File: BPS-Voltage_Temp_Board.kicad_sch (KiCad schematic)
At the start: 64 parts, among them J1 bms i2c test, J10 psom bms i2c test, J11 I-CAN connector, J2 voltage taps, J4 I-CAN connector, SW1 BMS_BOOT, SW2 SW_DIP_x05, U2 BQ7692003PW, U3 PeripheralSOM, U4 ISO1641BDR, U5 EL3H7, U6 EL3H7

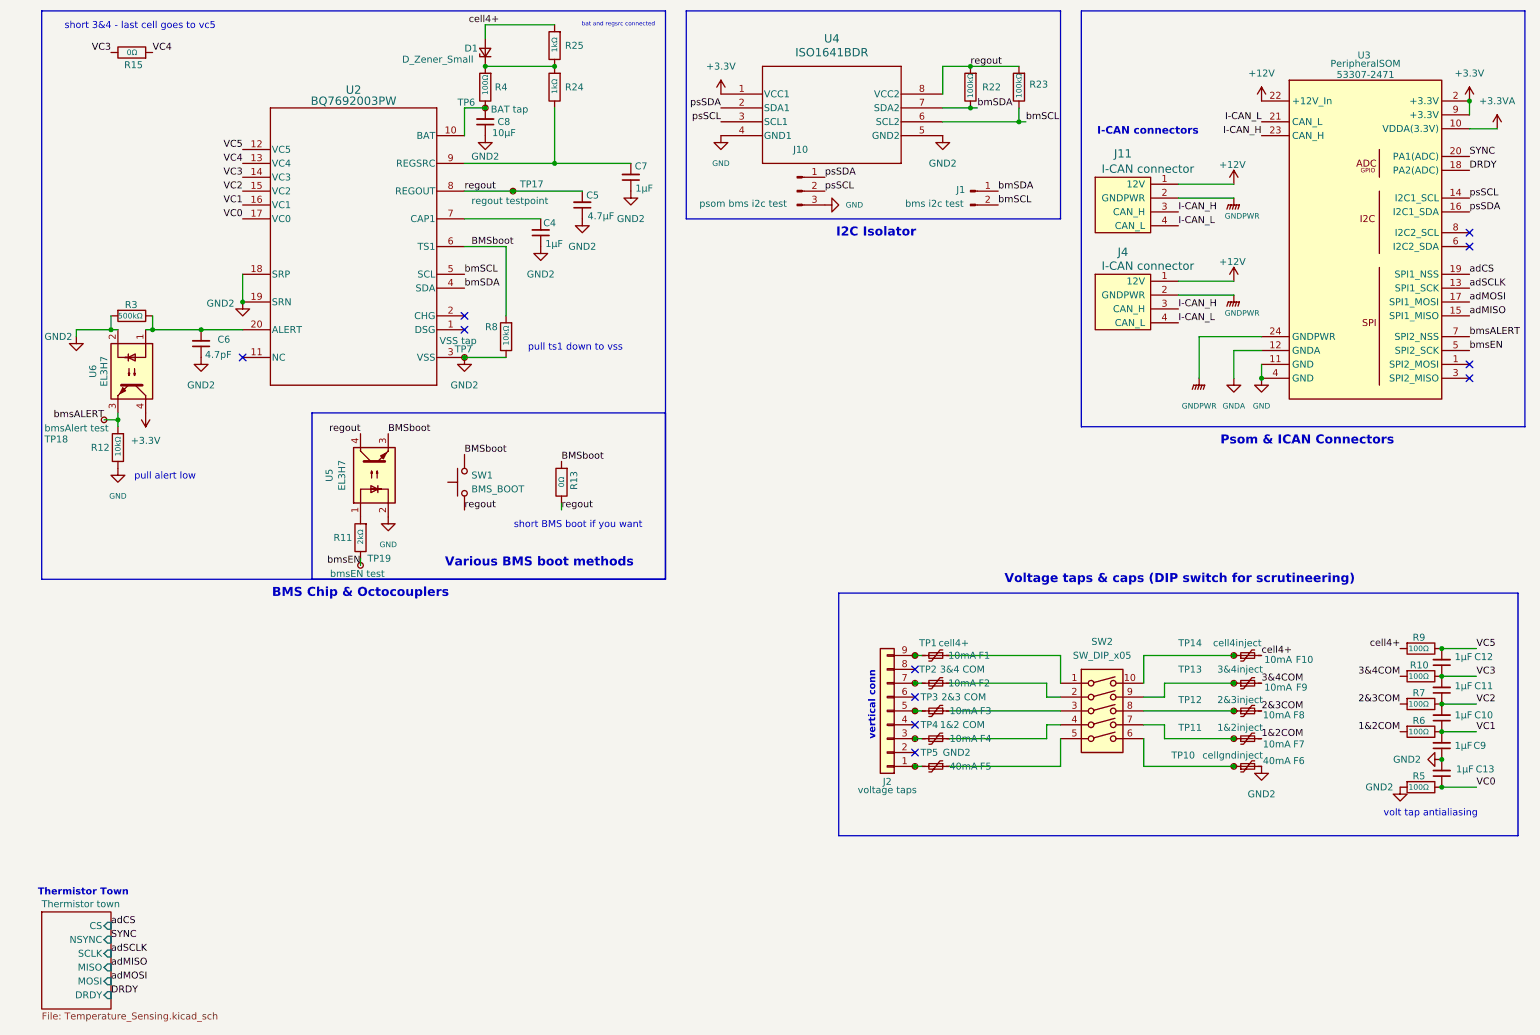
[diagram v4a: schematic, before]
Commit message: concerns from review council addressed
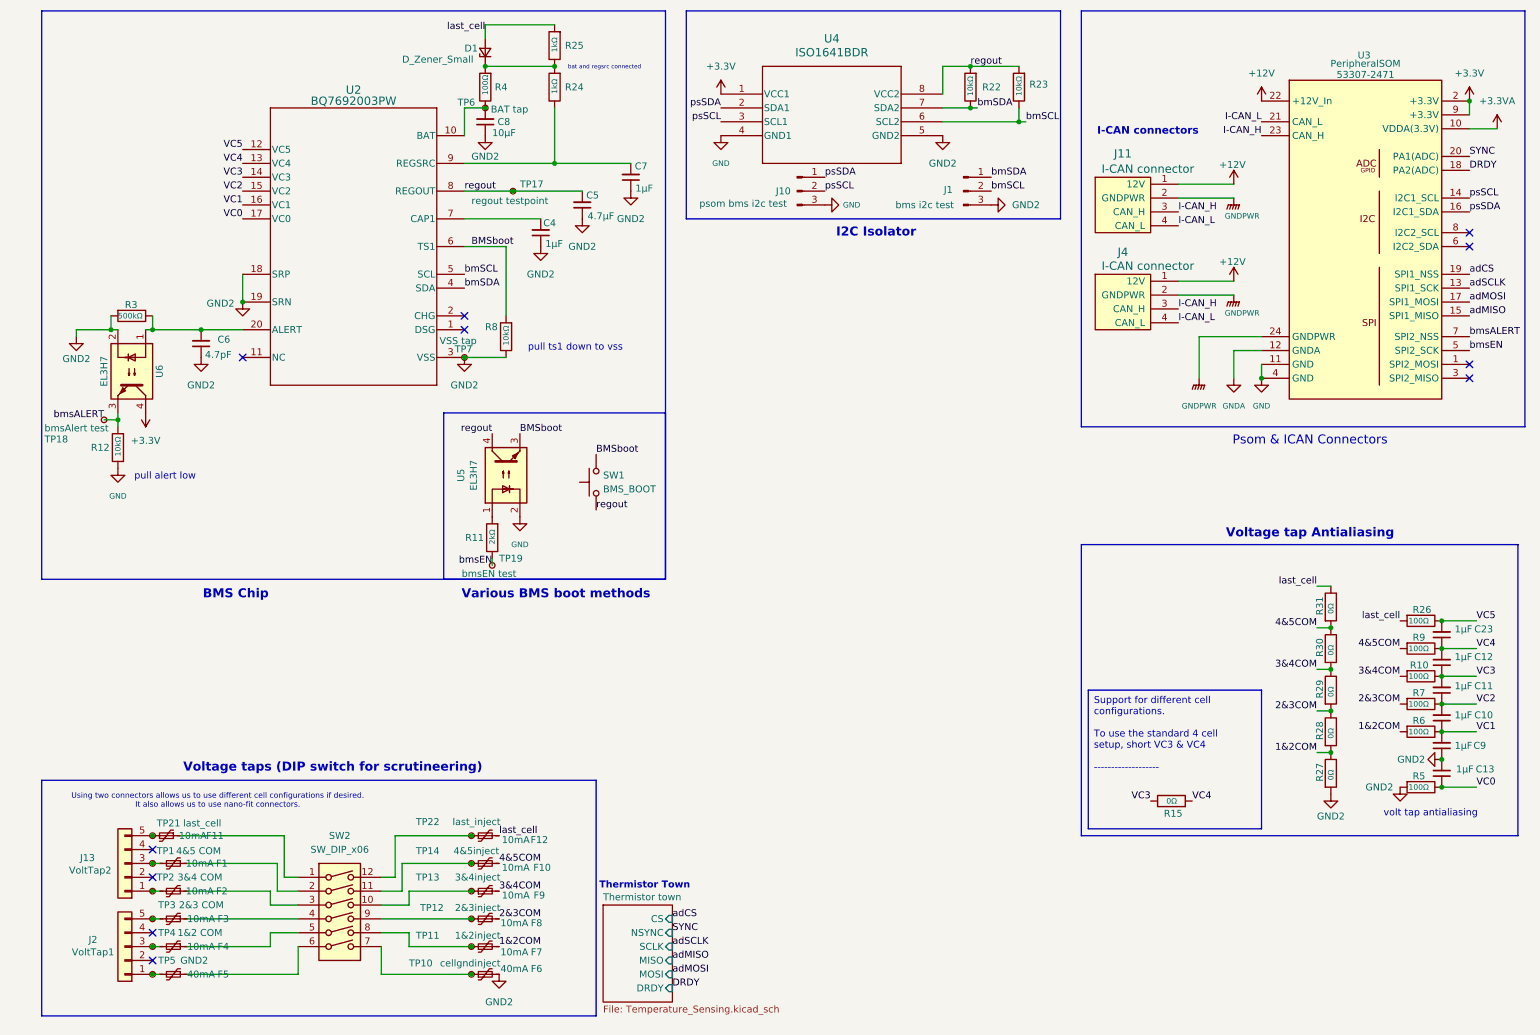
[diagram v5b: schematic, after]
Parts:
- removed J1: bms i2c test, symbol Connector:Conn_01x02_Pin
- removed J2: voltage taps, Connector_Molex:Molex_Nano-Fit_105314-xx10_2x05_P2.50mm_Horizontal, symbol Connector_Generic:Conn_01x09
- removed R13: 0Ω, Resistor_SMD:R_0805_2012Metric, symbol Device:R
- removed SW2: SW_DIP_x05, symbol Switch:SW_DIP_x05
- added C23: 1μF, Capacitor_SMD:C_0805_2012Metric, symbol Device:C_Small
- added F11, F12: 10mA, UTSVT_Special:ptc_fuse_FUSC1607X75N, symbol Device:Polyfuse_Small
- added J1: bms i2c test, symbol Connector:Conn_01x03_Pin
- added J13: VoltTap2, symbol Connector_Generic:Conn_01x05
- added J2: VoltTap1, symbol Connector_Generic:Conn_01x05
- added R26: 100Ω, Resistor_SMD:R_0805_2012Metric, symbol Device:R
- added R27, R28, R29, R30, R31: 0Ω, Resistor_SMD:R_0805_2012Metric, symbol Device:R
- added SW2: SW_DIP_x06, symbol Switch:SW_DIP_x06
- added TP21: last_cell, symbol Connector:TestPoint_Small
- added TP22: last_inject, symbol Connector:TestPoint_Small
- R22, R23: value 100kΩ -> 10kΩ
- TP1: value cell4+ -> 4&5 COM
- TP14: value cell4inject -> 4&5inject
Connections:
- net 1&2COM: now also R27.1, R28.2
- net 2&3COM: now also R28.1, R29.2
- net 3&4COM: now also R29.1, R30.2
- net GND2: now also J1.3 (Pin_3), R27.2
- net VC4: now also C12.2, R9.1, C23.1
- net VC5: now also C23.2, R26.1; no longer C12.2, R9.1
- net bmSCL: now also J1.2 (Pin_2)
- net bmSDA: now also J1.1 (Pin_1)
- net at F1.1: now also SW2.2
- net at F10.1, TP14.1: now also SW2.11
- net at F2.1: now also SW2.3
- net at F3.1: now also SW2.4
- net at F4.1: now also SW2.5
- net at F5.1: now also SW2.6
- net at F6.1, TP10.1: now also SW2.7
- net at F7.1, TP11.1: now also SW2.8
- net at F8.1, TP12.1: now also SW2.9
- net at F9.1, TP13.1: now also SW2.10
- net at F5.2, TP5.1: now also J2.1 (Pin_1)
- net at F2.2, TP2.1: now also J13.1 (Pin_1)
- net at F1.2, TP1.1: now also J13.3 (Pin_3)
- net at F4.2, TP4.1: now also J2.3 (Pin_3)
- net at F3.2, TP3.1: now also J2.5 (Pin_5)
- net cell4+ renamed 4&5COM
- net 4&5COM: now also R30.1, R31.2; no longer D1.2 (A), R25.2
- new net: F11.1, SW2.1
- new net: F12.1, SW2.12, TP22.1
- new net: F11.2, J13.5 (Pin_5), TP21.1
- new net last_cell: D1.2 (A), F12.2, R25.2, R26.2, R31.1
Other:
- note added: "BMS Chip"
- note added: "Using two connectors allows us to use different cell configurations if desired. It also allows us to use nano-fit connectors."
- note added: "Voltage tap Antialiasing"
- note added: "Voltage taps (DIP switch for scrutineering)"
- note removed: "BMS Chip & Octocouplers"
- note removed: "Voltage taps & caps (DIP switch for scrutineering)"
- note removed: "short 3&4 - last cell goes to vc5"
- note removed: "short BMS boot if you want"
- note removed: "vertical conn"
- company: (none) -> LHR Solar: Battery Protection System
- moved on the sheet: F1, F10, F2, F3, F4, F5, F6, F7, F8, F9, R11, R15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

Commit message: schematic should be finished. Preliminary layout with changes from review
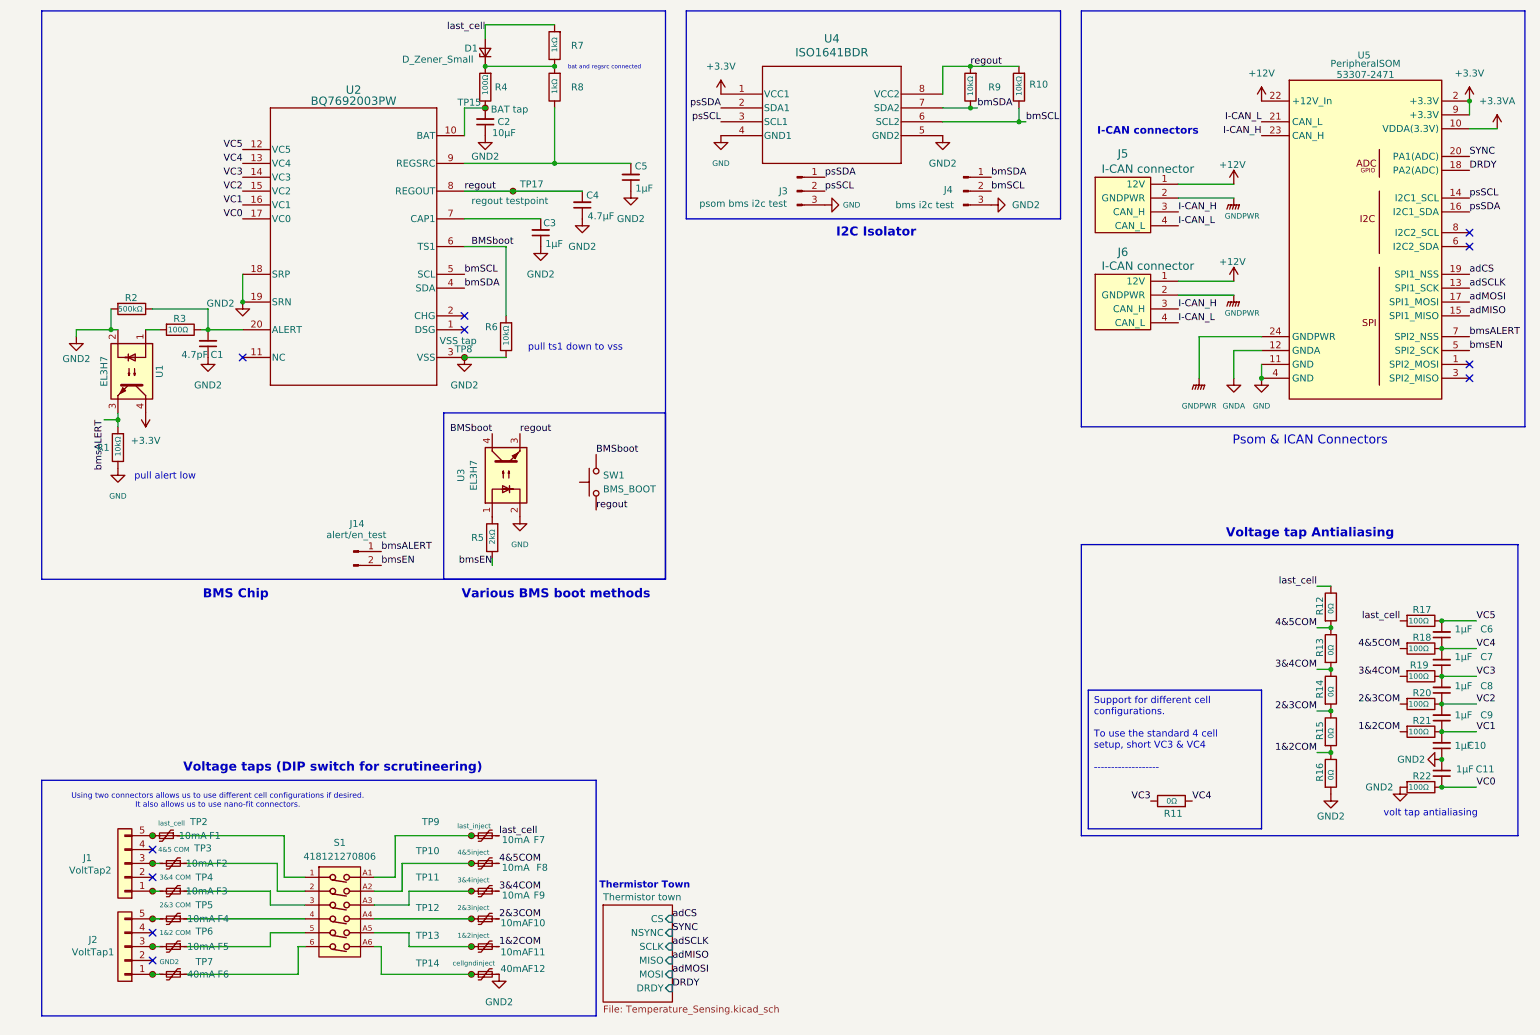
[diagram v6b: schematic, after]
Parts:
- removed SW2: SW_DIP_x06, symbol Switch:SW_DIP_x06
- removed TP18: bmsAlert test, symbol Connector:TestPoint_Small
- removed TP19: bmsEN test, symbol Connector:TestPoint_Small
- added J14: alert/en_test, Connector_PinHeader_2.54mm:PinHeader_1x02_P2.54mm_Vertical, symbol Connector:Conn_01x02_Pin
- added R3: 100Ω, Resistor_SMD:R_0805_2012Metric, symbol Device:R
- added S1: 418121270806, footprints:418121270806, symbol 418121270806:418121270806
- D1: footprint (none) -> Diode_SMD:D_0805_2012Metric
- J1: renamed from J13; footprint (none) -> Connector_Molex:Molex_Nano-Fit_105313-xx05_1x05_P2.50mm_Horizontal
- J2: footprint (none) -> Connector_Molex:Molex_Nano-Fit_105313-xx05_1x05_P2.50mm_Horizontal
- J3: renamed from J10; footprint (none) -> Connector_PinHeader_2.54mm:PinHeader_1x03_P2.54mm_Vertical
- J4: renamed from J1; footprint (none) -> Connector_PinHeader_2.54mm:PinHeader_1x03_P2.54mm_Vertical
- J5: renamed from J11; footprint UTSVT_Connectors:Molex_MicroFit3.0_1x4xP3.00mm_PolarizingPeg_Vertical -> Connector_Molex:Molex_Nano-Fit_105313-xx04_1x04_P2.50mm_Horizontal
- J6: renamed from J4; footprint UTSVT_Connectors:Molex_MicroFit3.0_1x4xP3.00mm_PolarizingPeg_Vertical -> Connector_Molex:Molex_Nano-Fit_105313-xx04_1x04_P2.50mm_Horizontal
- TP10: renamed from TP14; footprint (none) -> TestPoint:TestPoint_Keystone_5010-5014_Multipurpose
- TP11: renamed from TP13; footprint (none) -> TestPoint:TestPoint_Keystone_5010-5014_Multipurpose
- TP12: footprint (none) -> TestPoint:TestPoint_Keystone_5010-5014_Multipurpose
- TP13: renamed from TP11; footprint (none) -> TestPoint:TestPoint_Keystone_5010-5014_Multipurpose
- TP14: renamed from TP10; footprint (none) -> TestPoint:TestPoint_Keystone_5010-5014_Multipurpose
- TP15: renamed from TP6; footprint (none) -> UTSVT_Special:TestPoint_HEX_3mmID
- TP17: footprint (none) -> UTSVT_Special:TestPoint_HEX_3mmID
- TP2: renamed from TP21; footprint (none) -> UTSVT_Special:TestPoint_HEX_3mmID
- TP3: renamed from TP1; footprint (none) -> UTSVT_Special:TestPoint_HEX_3mmID
- TP4: renamed from TP2; footprint (none) -> UTSVT_Special:TestPoint_HEX_3mmID
- TP5: renamed from TP3; footprint (none) -> UTSVT_Special:TestPoint_HEX_3mmID
- TP6: renamed from TP4; footprint (none) -> UTSVT_Special:TestPoint_HEX_3mmID
- TP7: renamed from TP5; footprint (none) -> UTSVT_Special:TestPoint_HEX_3mmID
- TP8: renamed from TP7; footprint (none) -> UTSVT_Special:TestPoint_HEX_3mmID
- TP9: renamed from TP22; footprint (none) -> TestPoint:TestPoint_Keystone_5010-5014_Multipurpose
- renumbered C6 to C1, C9 to C10, C13 to C11, C8 to C2, C4 to C3, C5 to C4, C7 to C5, C23 to C6, C12 to C7, C11 to C8, C10 to C9, F11 to F1, F8 to F10, F7 to F11, F6 to F12, F1 to F2, F2 to F3, F3 to F4, F4 to F5, F5 to F6, F12 to F7, F10 to F8, R12 to R1, R23 to R10, R15 to R11, R31 to R12, R30 to R13, R29 to R14, R28 to R15, R27 to R16, R26 to R17, R9 to R18, R10 to R19, R3 to R2, R7 to R20, R6 to R21, R5 to R22, R11 to R5, R8 to R6, R25 to R7, R24 to R8, R22 to R9, U6 to U1, U5 to U3, U3 to U5
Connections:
- net BMSboot: now also U3.4; no longer U3.3
- net bmsALERT: now also J14.1 (Pin_1)
- net bmsEN: now also J14.2 (Pin_2)
- net regout: now also U3.3; no longer U3.4
- net at C1.2, R2.1, U2.20 (ALERT): now also R3.1; no longer U1.1
- net at F10.1, TP12.1: now also S1.A4
- net at F6.1: now also S1.6
- net at F1.1: now also S1.1
- net at F9.1, TP11.1: now also S1.A3
- net at F8.1, TP10.1: now also S1.A2
- net at F7.1, TP9.1: now also S1.A1
- net at F2.1: now also S1.2
- net at F3.1: now also S1.3
- net at F4.1: now also S1.4
- net at F5.1: now also S1.5
- net at F12.1, TP14.1: now also S1.A6
- net at F11.1, TP13.1: now also S1.A5
- new net: R3.2, U1.1
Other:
- moved on the sheet: C1, R2

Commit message: 1st layout done. silkscreen done. BOM added.
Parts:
- C1: P/N (none) -> 581-08052U4.7B
- C10, C11, C3, C5, C6, C7, C8, C9: P/N (none) -> C0805C105K5PACTU
- C2: P/N (none) -> TMK212BBJ106MGHT
- C4: P/N (none) -> C0805C475K3RACAUTO
- D1: P/N (none) -> 1N448W
- F1, F10, F11, F12, F2, F3, F4, F5, F6, F7, F8, F9: P/N (none) -> FUSC1607X75N
- J1, J2: P/N (none) -> 538-105313-1205
- J3, J4: P/N (none) -> 538-105313-1103
- J5, J6: P/N 436500244 -> 538-105313-2104
- R1, R10, R6, R9: P/N (none) -> CRCW080510K0FKEAC
- R11, R12, R13, R14, R15, R16: P/N (none) -> SMD_0805
- R17, R18, R19, R20, R21, R22, R3, R4: P/N (none) -> 594-MCU0805MD1000BP1
- R2: P/N (none) -> 708-RNCF0805BTE500K
- R5: P/N (none) -> 667-ERJ-UP6D2001V
- R7, R8: P/N (none) -> CRCW08051K00FKEAC
- S1: P/N (none) -> 710-418121270806
- SW1: P/N (none) -> 653-B3SL-1002P
- U2: P/N (none) -> 595-BQ7692000PWR
- U4: P/N (none) -> 595-ADS131M08QPBSRQ1
